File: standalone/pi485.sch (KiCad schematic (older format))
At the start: 27 parts, among them J1 RS485, P1 Rasperry Pi, P2 PWR, P3 Term, P4 Latch Disable, Q1 2N4401, Q2 2N4401, Q3 2N4401, U1 NE555, U2 MAX485

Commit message: Renamed bearer.
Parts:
- C1, C2, C3: symbol CAP -> C
- D4: symbol DIODE -> D
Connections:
- wire segments 74 -> 105
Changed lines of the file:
@@
 LIBS:zetex
 LIBS:Zilog
-LIBS:pi485-cache
 EELAYER 26 0
 EELAYER END
@@
 $EndComp
 $Comp
-L CAP C3
+L C C3
 U 1 1 586E89BC
 P 6150 5450
@@
 $EndComp
 $Comp
-L CAP C2
+L C C2
 U 1 1 5876F3DF
 P 7050 1400
@@
 $EndComp
 $Comp
-L CAP C1
+L C C1
 U 1 1 5876F5F2
 P 6600 1400
@@
 $EndComp
 $Comp
-L DIODE D4
+L D D4
 U 1 1 5879650D
 P 5850 4400
@@
 Connection ~ 2150 2150
 Wire Wire Line
-	2600 2150 2600 3200
+	2600 2150 2600 2900
+Wire Wire Line
+	2600 2900 2600 3200
 Wire Wire Line
 	2600 2900 2150 2900
 Wire Wire Line
-	5500 3550 5500 4450
-Wire Wire Line
-	6400 4300 6400 5450
+	5500 3550 5500 3800
+Wire Wire Line
+	5500 3800 5500 4450
+Wire Wire Line
+	6400 4300 6400 4400
+Wire Wire Line
+	6400 4400 6400 4850
+Wire Wire Line
+	6400 4850 6400 5050
+Wire Wire Line
+	6400 5050 6400 5450
 Wire Wire Line
 	6400 4850 6000 4850
@@
 Connection ~ 6400 4850
 Wire Wire Line
-	5000 5450 5900 5450
-Wire Wire Line
-	5500 5250 5500 5650
+	5000 5450 5500 5450
+Wire Wire Line
+	5500 5450 6000 5450
+Wire Wire Line
+	5500 5250 5500 5450
+Wire Wire Line
+	5500 5450 5500 5650
 Connection ~ 5500 5450
 Wire Wire Line
@@
 	2150 2800 2500 2800
 Wire Wire Line
-	2500 2150 2500 3200
-Wire Wire Line
-	2150 1850 2150 2800
-Wire Wire Line
-	2150 2900 2150 3250
+	2500 2150 2500 2800
+Wire Wire Line
+	2500 2800 2500 3200
+Wire Wire Line
+	2150 1850 2150 2150
+Wire Wire Line
+	2150 2150 2150 2800
+Wire Wire Line
+	2150 2900 2150 3050
+Wire Wire Line
+	2150 3050 2150 3250
 Connection ~ 2150 3050
 Wire Wire Line
 	2700 2150 2700 3100
 Wire Wire Line
-	4850 3100 4850 4650
+	4850 3100 4850 4400
+Wire Wire Line
+	4850 4400 4850 4650
 Connection ~ 6400 4400
 Wire Wire Line
 	2800 3000 2800 2150
 Wire Wire Line
-	2700 3100 6550 3100
+	2700 3100 3100 3100
+Wire Wire Line
+	3100 3100 4850 3100
+Wire Wire Line
+	4850 3100 6550 3100
 Wire Wire Line
 	4850 4650 5000 4650
@@
 	6700 2600 6650 2600
 Wire Wire Line
-	6650 2600 6650 4650
+	6650 2600 6650 2900
+Wire Wire Line
+	6650 2900 6650 4650
 Wire Wire Line
 	6650 2900 6700 2900
@@
 	8000 2300 8000 2200
 Wire Wire Line
-	8000 2800 8000 3000
-Wire Wire Line
-	2800 3000 6450 3000
+	8000 2800 8000 2900
+Wire Wire Line
+	8000 2900 8000 3000
+Wire Wire Line
+	2800 3000 4000 3000
+Wire Wire Line
+	4000 3000 6450 3000
 Wire Wire Line
 	6450 3000 6450 2500
@@
 	7500 2650 7500 2300
 Wire Wire Line
-	7500 2300 9000 2300
+	7500 2300 8000 2300
+Wire Wire Line
+	8000 2300 9000 2300
 Wire Wire Line
 	9000 2300 9000 2500
@@
 	7500 2850 7500 2900
 Wire Wire Line
-	7500 2900 9000 2900
+	7500 2900 8000 2900
+Wire Wire Line
+	8000 2900 9000 2900
 Wire Wire Line
 	9000 2900 9000 2700
@@
 Connection ~ 2600 2900
 Wire Wire Line
-	4700 3800 6400 3800
+	4700 3800 5500 3800
+Wire Wire Line
+	5500 3800 6400 3800
 Wire Wire Line
 	6400 3800 6400 4000
 Wire Wire Line
-	5650 4400 4850 4400
+	5700 4400 4850 4400
 Wire Wire Line
 	2900 4300 2900 4850
 Wire Wire Line
-	2900 5150 2900 5550
+	2900 5150 2900 5400
+Wire Wire Line
+	2900 5400 2900 5550
 Wire Wire Line
 	2800 4300 2900 4300
 Wire Wire Line
-	2500 3550 2500 4500
+	2500 3550 2500 4300
+Wire Wire Line
+	2500 4300 2500 4500
 Wire Wire Line
 	2800 4500 3800 4500
@@
 Connection ~ 4000 3000
 Wire Wire Line
-	6050 4400 6400 4400
+	6000 4400 6400 4400
 Connection ~ 6400 5050
 Wire Wire Line
@@
 	5600 2900 5600 2750
 Wire Wire Line
-	5800 2000 7100 2000
+	5800 2000 6200 2000
+Wire Wire Line
+	6200 2000 6600 2000
+Wire Wire Line
+	6600 2000 7050 2000
+Wire Wire Line
+	7050 2000 7100 2000
 Wire Wire Line
 	7100 2000 7100 2300
 Wire Wire Line
-	6200 3550 6200 1700
+	6200 3550 6200 2000
+Wire Wire Line
+	6200 2000 6200 1700
 Wire Wire Line
 	8250 1000 8250 1900
 Connection ~ 6200 2000
 Wire Wire Line
-	2500 3550 6200 3550
-Wire Wire Line
-	6200 1000 8250 1000
+	2500 3550 5500 3550
+Wire Wire Line
+	5500 3550 6200 3550
+Wire Wire Line
+	6200 1000 6600 1000
+Wire Wire Line
+	6600 1000 7050 1000
+Wire Wire Line
+	7050 1000 8250 1000
 Wire Wire Line
 	6200 1000 6200 1100
 Wire Wire Line
-	2900 5400 4200 5400
-Wire Wire Line
-	6600 2000 6600 1650
-Wire Wire Line
-	7050 1650 7050 2000
+	2900 5400 3300 5400
+Wire Wire Line
+	3300 5400 3800 5400
+Wire Wire Line
+	3800 5400 4200 5400
+Wire Wire Line
+	6600 2000 6600 1550
+Wire Wire Line
+	7050 1550 7050 2000
 Connection ~ 7050 2000
 Wire Wire Line
-	7050 1150 7050 1000
+	7050 1250 7050 1000
 Connection ~ 7050 1000
 Wire Wire Line
-	6600 1150 6600 1000
+	6600 1250 6600 1000
 Connection ~ 6600 1000
 Connection ~ 6600 2000
@@
 	5600 2300 5600 2450
 Connection ~ 5500 3550
+Wire Wire Line
+	6400 5450 6300 5450
 $EndSCHEMATC

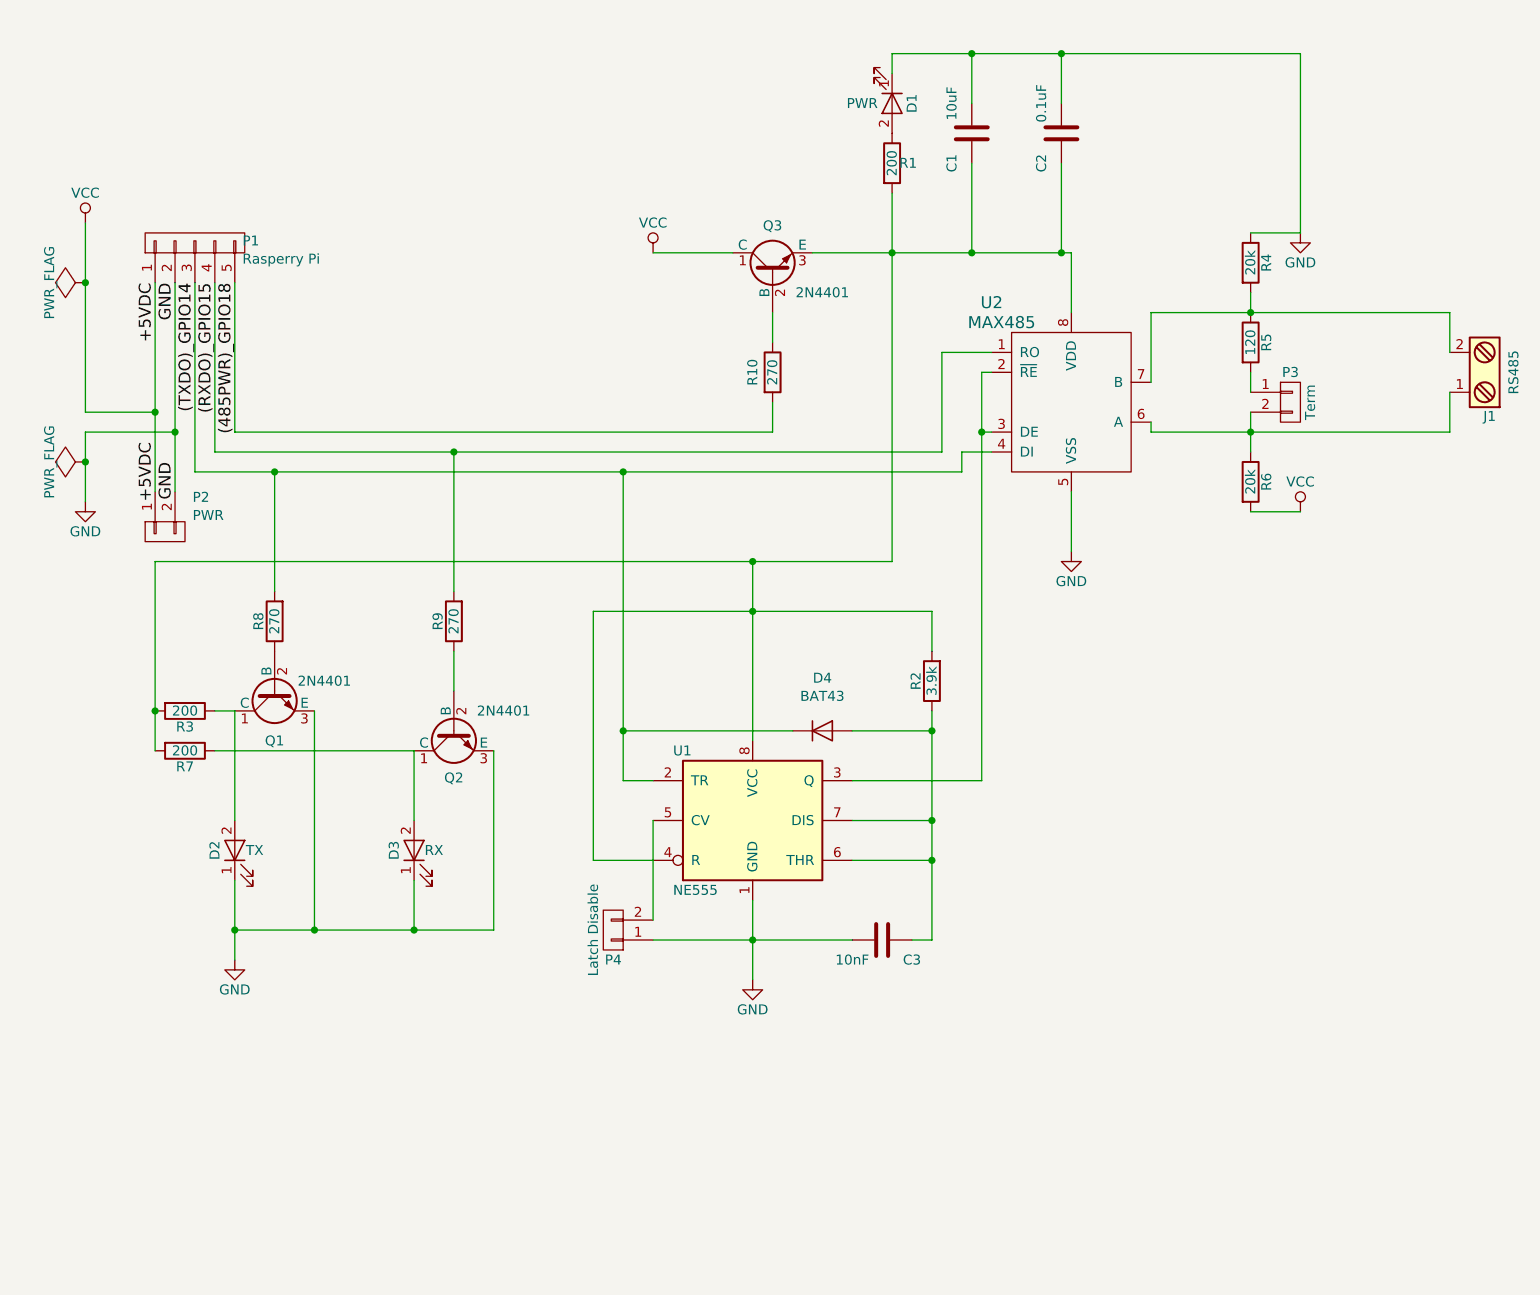
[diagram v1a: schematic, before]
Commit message: Updated with TERM / RO values in schemas and PCBs
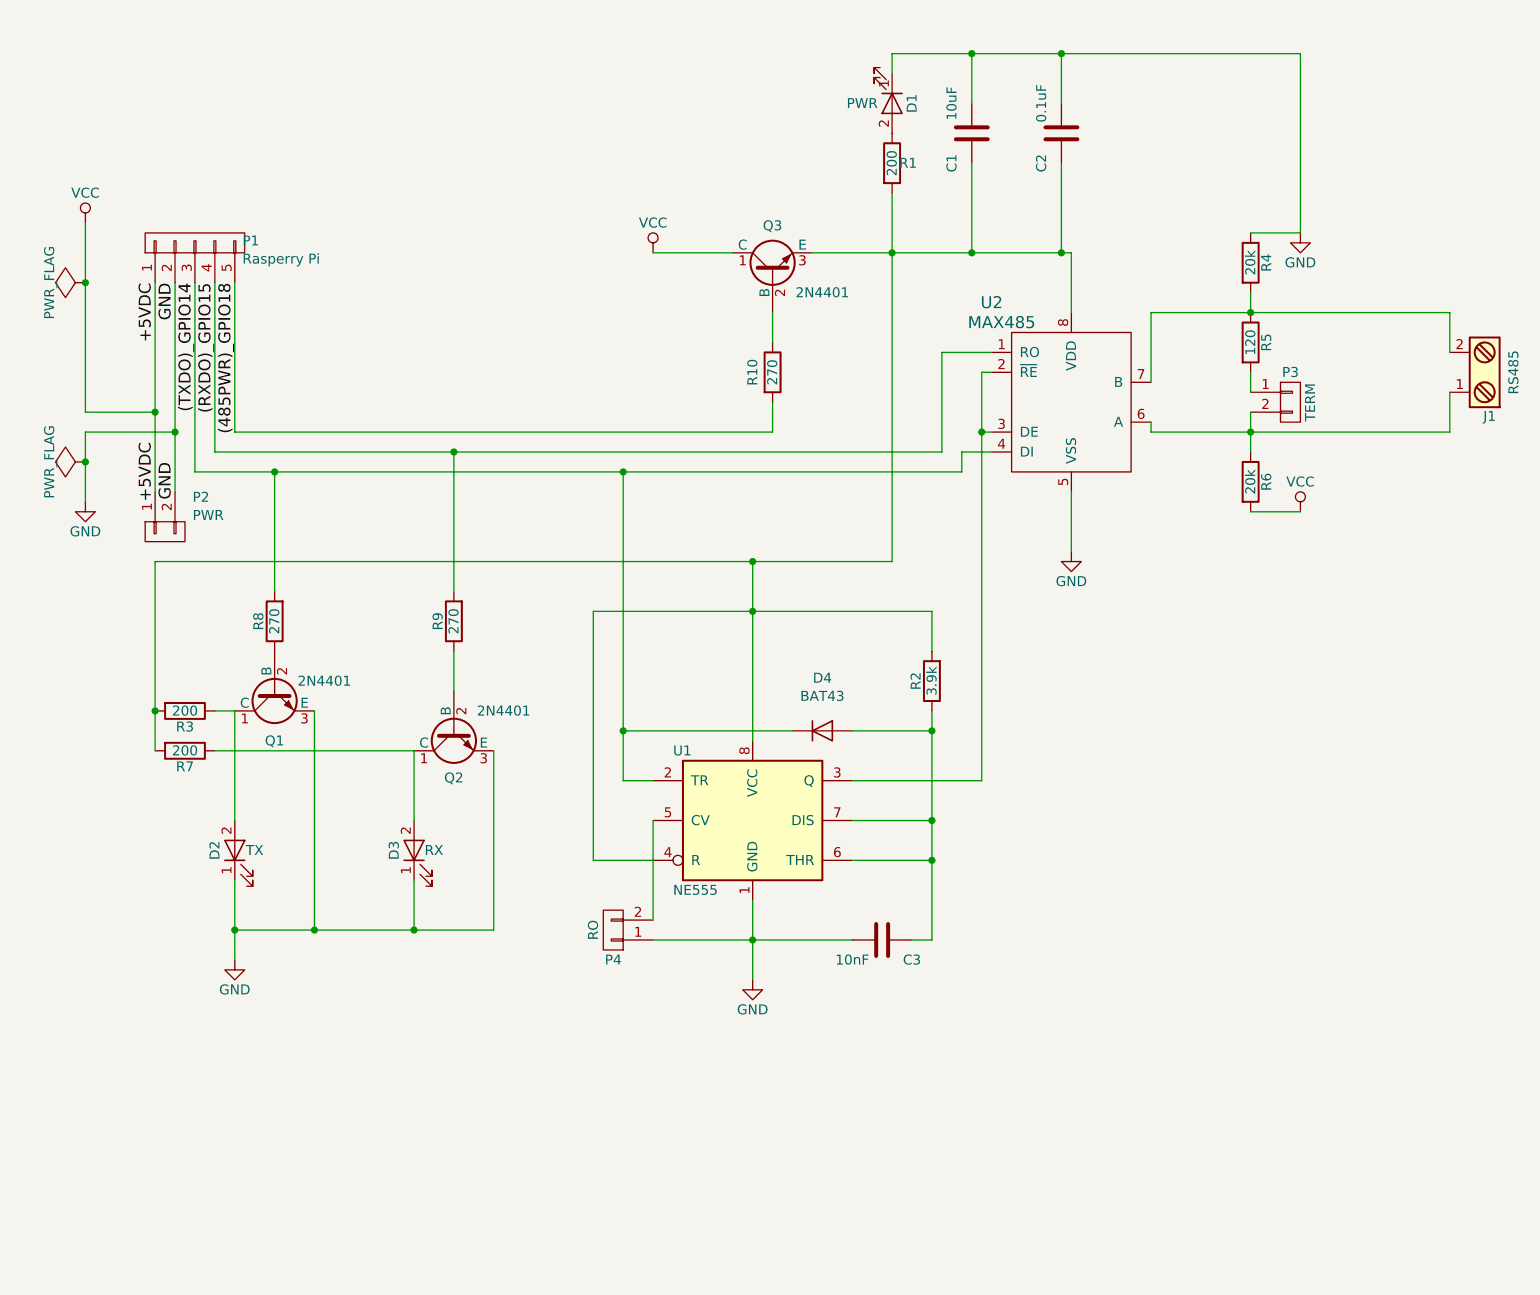
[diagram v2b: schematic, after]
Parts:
- P3: value Term -> TERM
- P4: value Latch Disable -> RO
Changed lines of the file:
@@
 LIBS:zetex
 LIBS:Zilog
+LIBS:pi485-cache
 EELAYER 26 0
 EELAYER END
@@
 $EndComp
 $Comp
-L GND #PWR06
+L GND #PWR05
 U 1 1 586E84AD
 P 2900 5550
-F 0 "#PWR06" H 2900 5300 50  0001 C CNN
+F 0 "#PWR05" H 2900 5300 50  0001 C CNN
 F 1 "GND" H 2900 5400 50  0000 C CNN
 F 2 "" H 2900 5550 50  0000 C CNN
@@
 $EndComp
 $Comp
-L GND #PWR07
+L GND #PWR06
 U 1 1 586E98F0
 P 5500 5650
-F 0 "#PWR07" H 5500 5400 50  0001 C CNN
+F 0 "#PWR06" H 5500 5400 50  0001 C CNN
 F 1 "GND" H 5500 5500 50  0000 C CNN
 F 2 "" H 5500 5650 50  0000 C CNN
@@
 $EndComp
 $Comp
-L GND #PWR08
+L GND #PWR07
 U 1 1 586EB44F
 P 7100 3500
-F 0 "#PWR08" H 7100 3250 50  0001 C CNN
+F 0 "#PWR07" H 7100 3250 50  0001 C CNN
 F 1 "GND" H 7100 3350 50  0000 C CNN
 F 2 "" H 7100 3500 50  0000 C CNN
@@
 $EndComp
 $Comp
-L VCC #PWR09
+L VCC #PWR08
 U 1 1 586EB484
 P 5000 2000
-F 0 "#PWR09" H 5000 1850 50  0001 C CNN
+F 0 "#PWR08" H 5000 1850 50  0001 C CNN
 F 1 "VCC" H 5000 2150 50  0000 C CNN
 F 2 "" H 5000 2000 50  0000 C CNN
@@
 P 8200 2750
 F 0 "P3" H 8200 2900 50  0000 C CNN
-F 1 "Term" V 8300 2750 50  0000 C CNN
+F 1 "TERM" V 8300 2750 50  0000 C CNN
 F 2 "Pin_Headers:Pin_Header_Straight_1x02" H 8850 3000 50  0001 C CNN
 F 3 "" H 8200 2750 50  0000 C CNN
@@
 GND
 $Comp
-L GND #PWR010
+L GND #PWR09
 U 1 1 586F0172
 P 8250 1900
-F 0 "#PWR010" H 8250 1650 50  0001 C CNN
+F 0 "#PWR09" H 8250 1650 50  0001 C CNN
 F 1 "GND" H 8250 1750 50  0000 C CNN
 F 2 "" H 8250 1900 50  0000 C CNN
@@
 $EndComp
 $Comp
-L VCC #PWR011
+L VCC #PWR010
 U 1 1 586F01EA
 P 8250 3300
-F 0 "#PWR011" H 8250 3150 50  0001 C CNN
+F 0 "#PWR010" H 8250 3150 50  0001 C CNN
 F 1 "VCC" H 8250 3450 50  0000 C CNN
 F 2 "" H 8250 3300 50  0000 C CNN
@@
 P 4800 5400
 F 0 "P4" H 4800 5550 50  0000 C CNN
-F 1 "Latch Disable" V 4900 5400 50  0000 C CNN
+F 1 "RO" V 4900 5400 50  0000 C CNN
 F 2 "Pin_Headers:Pin_Header_Straight_1x02" H 5450 5650 50  0001 C CNN
 F 3 "" H 4800 5400 50  0000 C CNN
@@
 Connection ~ 2150 2150
 Wire Wire Line
-	2600 2150 2600 2900
-Wire Wire Line
-	2600 2900 2600 3200
+	2600 2150 2600 3200
 Wire Wire Line
 	2600 2900 2150 2900
 Wire Wire Line
-	5500 3550 5500 3800
-Wire Wire Line
-	5500 3800 5500 4450
-Wire Wire Line
-	6400 4300 6400 4400
-Wire Wire Line
-	6400 4400 6400 4850
-Wire Wire Line
-	6400 4850 6400 5050
-Wire Wire Line
-	6400 5050 6400 5450
+	5500 3550 5500 4450
+Wire Wire Line
+	6400 4300 6400 5450
 Wire Wire Line
 	6400 4850 6000 4850
@@
 Connection ~ 6400 4850
 Wire Wire Line
-	5000 5450 5500 5450
-Wire Wire Line
-	5500 5450 6000 5450
-Wire Wire Line
-	5500 5250 5500 5450
-Wire Wire Line
-	5500 5450 5500 5650
+	5000 5450 6000 5450
+Wire Wire Line
+	5500 5250 5500 5650
 Connection ~ 5500 5450
 Wire Wire Line
@@
 	2150 2800 2500 2800
 Wire Wire Line
-	2500 2150 2500 2800
-Wire Wire Line
-	2500 2800 2500 3200
-Wire Wire Line
-	2150 1850 2150 2150
-Wire Wire Line
-	2150 2150 2150 2800
-Wire Wire Line
-	2150 2900 2150 3050
-Wire Wire Line
-	2150 3050 2150 3250
+	2500 2150 2500 3200
+Wire Wire Line
+	2150 1850 2150 2800
+Wire Wire Line
+	2150 2900 2150 3250
 Connection ~ 2150 3050
 Wire Wire Line
 	2700 2150 2700 3100
 Wire Wire Line
-	4850 3100 4850 4400
-Wire Wire Line
-	4850 4400 4850 4650
+	4850 3100 4850 4650
 Connection ~ 6400 4400
 Wire Wire Line
 	2800 3000 2800 2150
 Wire Wire Line
-	2700 3100 3100 3100
-Wire Wire Line
-	3100 3100 4850 3100
-Wire Wire Line
-	4850 3100 6550 3100
+	2700 3100 6550 3100
 Wire Wire Line
 	4850 4650 5000 4650
@@
 	6700 2600 6650 2600
 Wire Wire Line
-	6650 2600 6650 2900
-Wire Wire Line
-	6650 2900 6650 4650
+	6650 2600 6650 4650
 Wire Wire Line
 	6650 2900 6700 2900
@@
 	8000 2300 8000 2200
 Wire Wire Line
-	8000 2800 8000 2900
-Wire Wire Line
-	8000 2900 8000 3000
-Wire Wire Line
-	2800 3000 4000 3000
-Wire Wire Line
-	4000 3000 6450 3000
+	8000 2800 8000 3000
+Wire Wire Line
+	2800 3000 6450 3000
 Wire Wire Line
 	6450 3000 6450 2500
@@
 	7500 2650 7500 2300
 Wire Wire Line
-	7500 2300 8000 2300
-Wire Wire Line
-	8000 2300 9000 2300
+	7500 2300 9000 2300
 Wire Wire Line
 	9000 2300 9000 2500
@@
 	7500 2850 7500 2900
 Wire Wire Line
-	7500 2900 8000 2900
-Wire Wire Line
-	8000 2900 9000 2900
+	7500 2900 9000 2900
 Wire Wire Line
 	9000 2900 9000 2700
@@
 Connection ~ 2600 2900
 Wire Wire Line
-	4700 3800 5500 3800
-Wire Wire Line
-	5500 3800 6400 3800
+	4700 3800 6400 3800
 Wire Wire Line
 	6400 3800 6400 4000
@@
 	2900 4300 2900 4850
 Wire Wire Line
-	2900 5150 2900 5400
-Wire Wire Line
-	2900 5400 2900 5550
+	2900 5150 2900 5550
 Wire Wire Line
 	2800 4300 2900 4300
 Wire Wire Line
-	2500 3550 2500 4300
-Wire Wire Line
-	2500 4300 2500 4500
+	2500 3550 2500 4500
 Wire Wire Line
 	2800 4500 3800 4500
@@
 	5600 2900 5600 2750
 Wire Wire Line
-	5800 2000 6200 2000
-Wire Wire Line
-	6200 2000 6600 2000
-Wire Wire Line
-	6600 2000 7050 2000
-Wire Wire Line
-	7050 2000 7100 2000
+	5800 2000 7100 2000
 Wire Wire Line
 	7100 2000 7100 2300
 Wire Wire Line
-	6200 3550 6200 2000
-Wire Wire Line
-	6200 2000 6200 1700
+	6200 3550 6200 1700
 Wire Wire Line
 	8250 1000 8250 1900
 Connection ~ 6200 2000
 Wire Wire Line
-	2500 3550 5500 3550
-Wire Wire Line
-	5500 3550 6200 3550
-Wire Wire Line
-	6200 1000 6600 1000
-Wire Wire Line
-	6600 1000 7050 1000
-Wire Wire Line
-	7050 1000 8250 1000
+	2500 3550 6200 3550
+Wire Wire Line
+	6200 1000 8250 1000
 Wire Wire Line
 	6200 1000 6200 1100
 Wire Wire Line
-	2900 5400 3300 5400
-Wire Wire Line
-	3300 5400 3800 5400
-Wire Wire Line
-	3800 5400 4200 5400
+	2900 5400 4200 5400
 Wire Wire Line
 	6600 2000 6600 1550
